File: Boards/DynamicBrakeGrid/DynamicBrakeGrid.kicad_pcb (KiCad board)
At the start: 4 copper layers, 350 x 150 mm, 166 parts, among them IC1 ISO1042BDWVR, IC3 UCC27424QDRQ1, IC5 LM358DR, IC6 MCP2515-e_ST, IC8 LM358DR, J1 1987724, J10 5442251, J11 5442251, J12 5442251, J13 38969-0002, J14 5442251, J15 5442251, J18 38969-0002, J19 38969-0002, J2 1987724, J20 38969-0002, J21 38969-0002, J22 38969-0002, J24 5442251, J25 5442251, J5 5442251, J6 5442251, J7 5442251, J8 5442251, J9 5442251, M1 Fan_4pin, M10 Fan_4pin, M11 Fan_4pin, M12 Fan_4pin, M2 Fan_4pin, M3 Fan_4pin, M4 Fan_4pin, M5 Fan_4pin, M6 Fan_4pin, M7 Fan_4pin, M8 Fan_4pin, M9 Fan_4pin, U6 ACS758xCB-200U-PFF, Y1 8MHz

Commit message: Generate Bill of Materials
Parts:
- C2, C3, C4, C5, C6, C7, C8, C9: value 1000uF -> UVY1E102MPD1TD
- Q1: value ~ -> FZ400R12KE4
- R53: value 58 -> 10
- R71: value 120k -> 60k
- U6: value ACS758xCB-200U-PFF -> ACS758ECB-200U-PFF
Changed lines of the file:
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@@
 			)
 		)
-		(property "Value" "1000uF"
+		(property "Value" "UVY1E102MPD1TD"
 			(at 0.5 -11.5 0)
 			(layer "F.SilkS")
@@
 			)
 		)
-		(property "Value" "58"
+		(property "Value" "10"
 			(at 0 2.28 90)
 			(layer "F.Fab")
@@
 			)
 		)
-		(property "Value" "120k"
+		(property "Value" "60k"
 			(at 0 2.28 90)
 			(layer "F.Fab")
@@
 			)
 		)
-		(property "Value" "~"
+		(property "Value" "FZ400R12KE4"
 			(at 0 1 180)
 			(unlocked yes)
@@
 			)
 		)
-		(property "Value" "1000uF"
+		(property "Value" "UVY1E102MPD1TD"
 			(at 0.5 -11.5 0)
 			(layer "F.SilkS")
@@
 			)
 		)
-		(property "Value" "1000uF"
+		(property "Value" "UVY1E102MPD1TD"
 			(at 0.5 -11.5 0)
 			(layer "F.SilkS")
@@
 			)
 		)
-		(property "Value" "1000uF"
+		(property "Value" "UVY1E102MPD1TD"
 			(at 0.5 -11.5 0)
 			(layer "F.SilkS")
@@
 			)
 		)
-		(property "Value" "1000uF"
+		(property "Value" "UVY1E102MPD1TD"
 			(at 0.5 -11.5 0)
 			(layer "F.SilkS")
@@
 			)
 		)
-		(property "Value" "1000uF"
+		(property "Value" "UVY1E102MPD1TD"
 			(at 0.5 -11.5 0)
 			(layer "F.SilkS")
@@
 			)
 		)
-		(property "Value" "1000uF"
+		(property "Value" "UVY1E102MPD1TD"
 			(at 0.5 -11.5 0)
 			(layer "F.SilkS")
@@
 			)
 		)
-		(property "Value" "ACS758xCB-200U-PFF"
+		(property "Value" "ACS758ECB-200U-PFF"
 			(at 2.91 -9.7 0)
 			(layer "F.Fab")
@@
 			)
 		)
-		(property "Value" "1000uF"
+		(property "Value" "UVY1E102MPD1TD"
 			(at 0.5 -11.5 0)
 			(layer "F.SilkS")

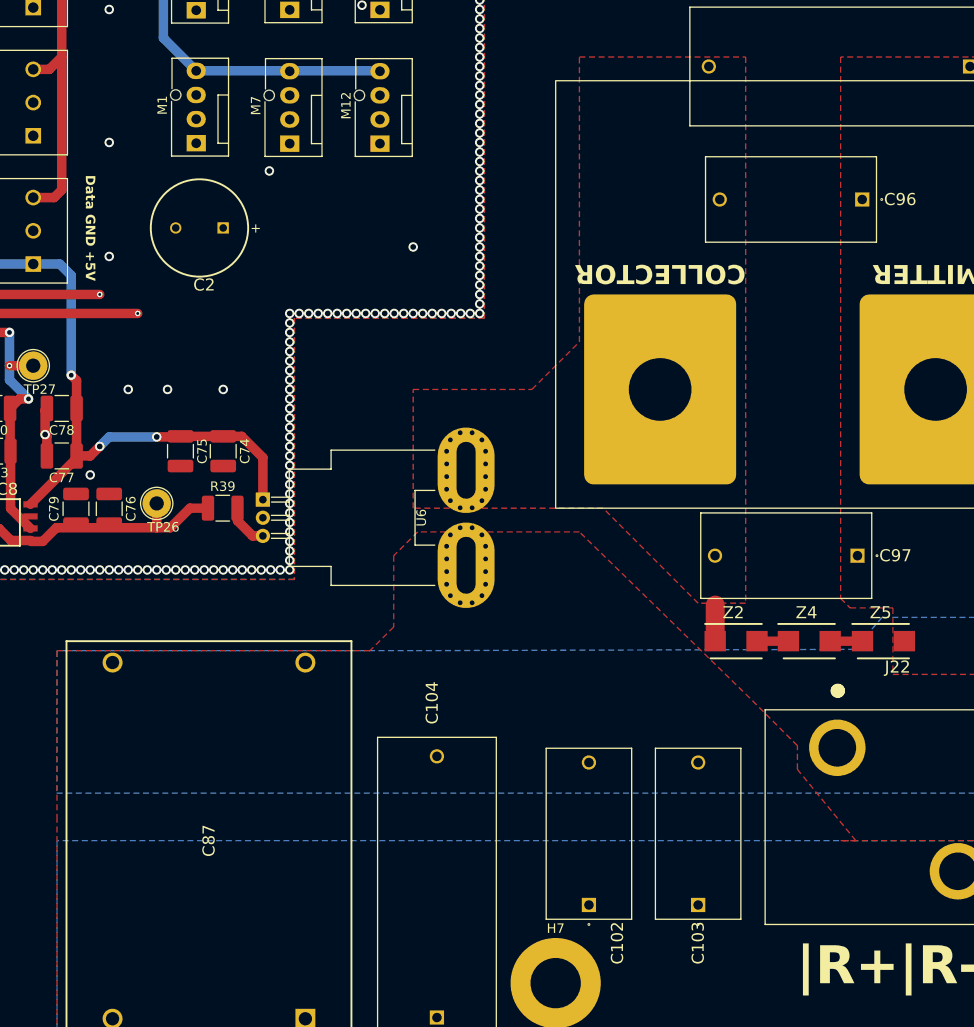
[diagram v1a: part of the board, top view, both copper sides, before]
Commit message: Update board soldermask
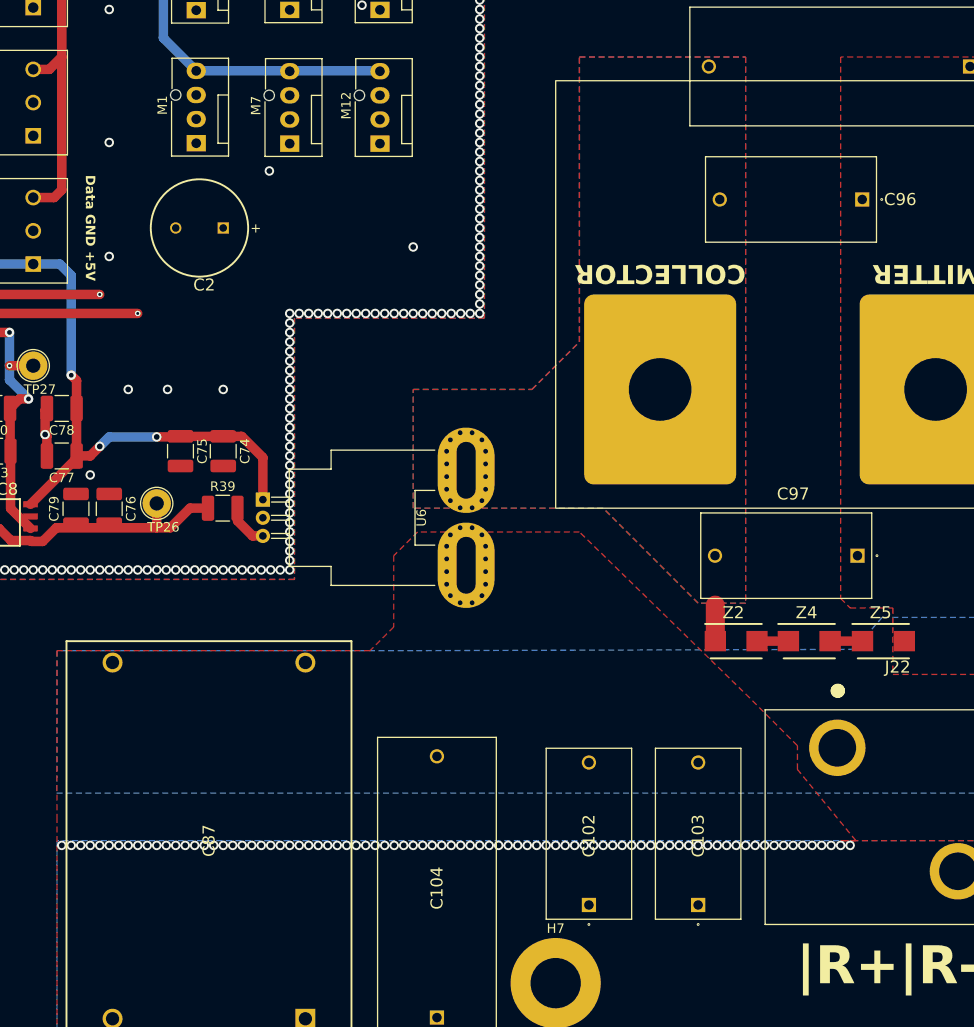
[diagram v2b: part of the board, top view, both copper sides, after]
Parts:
- moved REF** 165.1 mm to (103.0, 162.0)
- moved REF** 165.1 mm to (121.0, 161.0)
- moved REF** 165.1 mm to (88.0, 163.0)
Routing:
- net Net-(IC6-OSC1): track 24.2 -> 18.4 mm
- net RESISTOR_RETURN: vias 0 -> 84
- added copper zone on B.Cu, net CHOPPER_DRAIN
- added copper zone on In1.Cu, net CHOPPER_DRAIN
- added copper zone on In2.Cu, net CHOPPER_DRAIN
- added copper zone on In1.Cu, net GNDPWR
- added copper zone on In2.Cu, net GNDPWR
- added copper zone on In1.Cu, net RESISTOR_RETURN
- added copper zone on In2.Cu, net RESISTOR_RETURN
